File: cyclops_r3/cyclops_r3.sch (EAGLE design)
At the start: 133 parts, among them Q1 BC817, Q2 IRF510, U1 MCP4921, U10 TLV2374, U11 THS4281, U12 MAX4564, U13 ZXTD45, U14 ZXTD45, U2 ADG3301, U3 MCP4022-50k, U4 LT1931, U5 317-N, U6 337L, U7 TLV3701, U8 ADR03, U9 OP1177, X1 SLP3, X2 SLP3, X3 SLP3

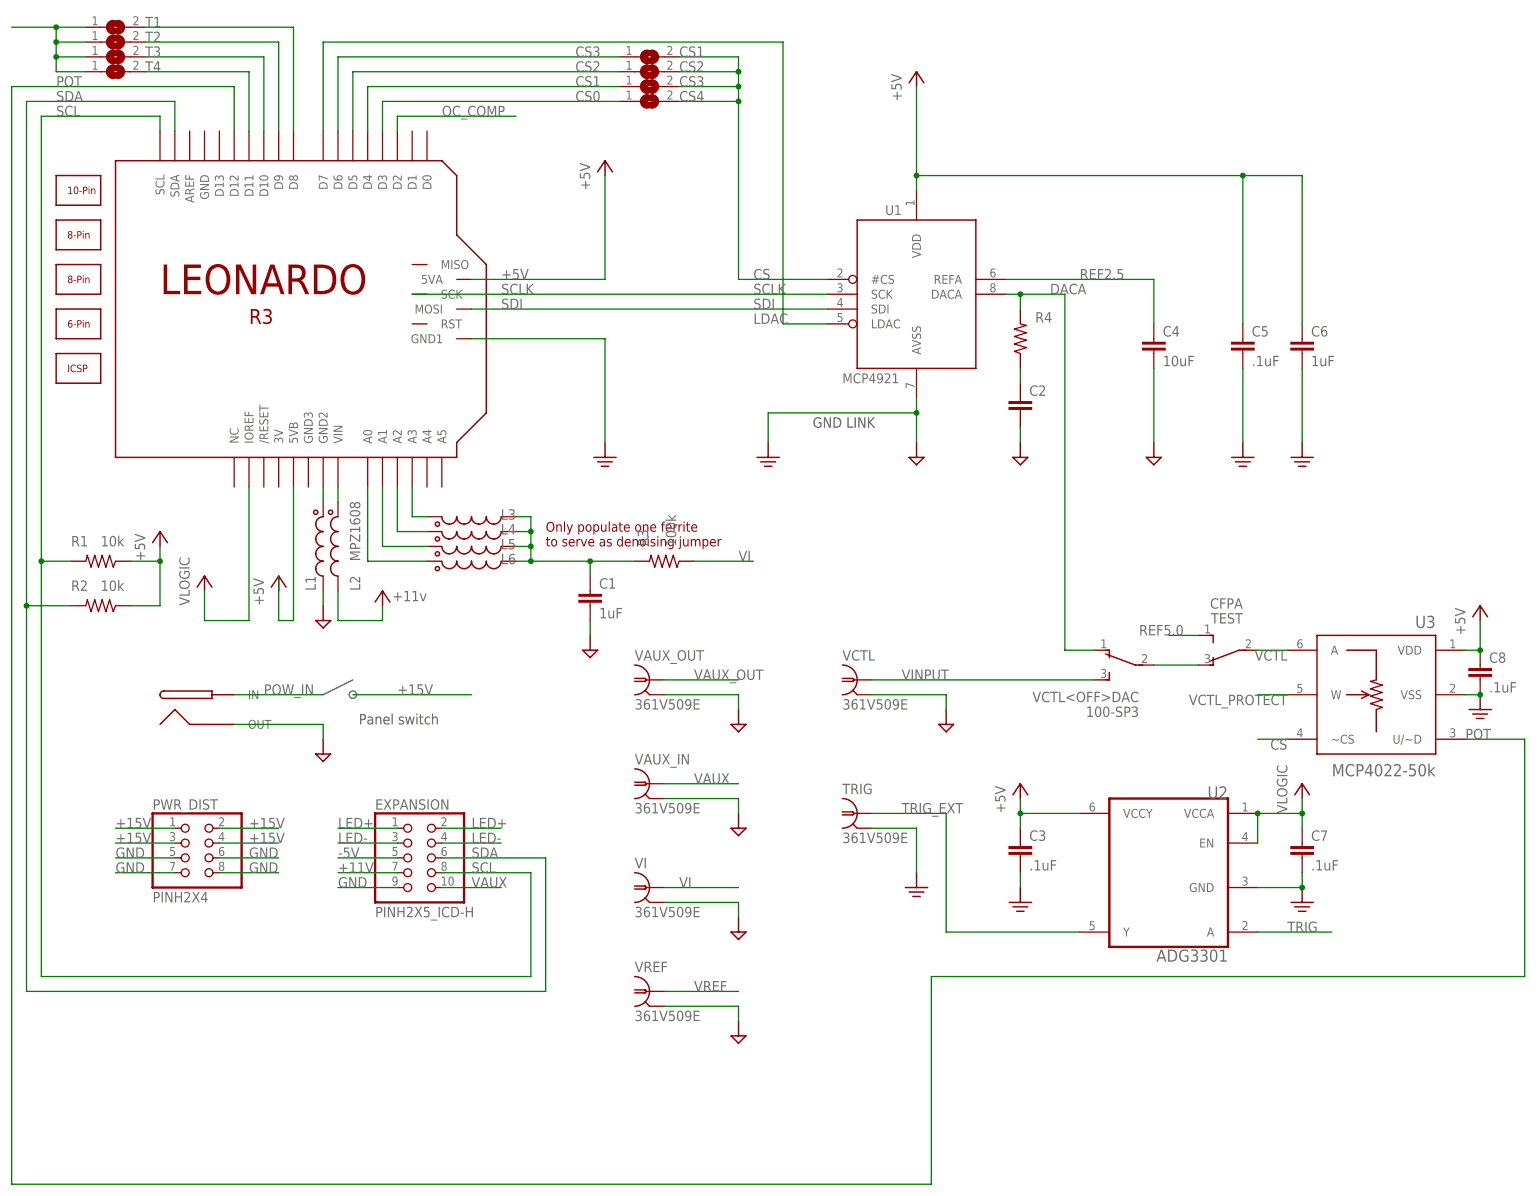
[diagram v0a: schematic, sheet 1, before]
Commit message: Almost ready to fabricate PCB. I need to do one last look over, concentrating on schematic.
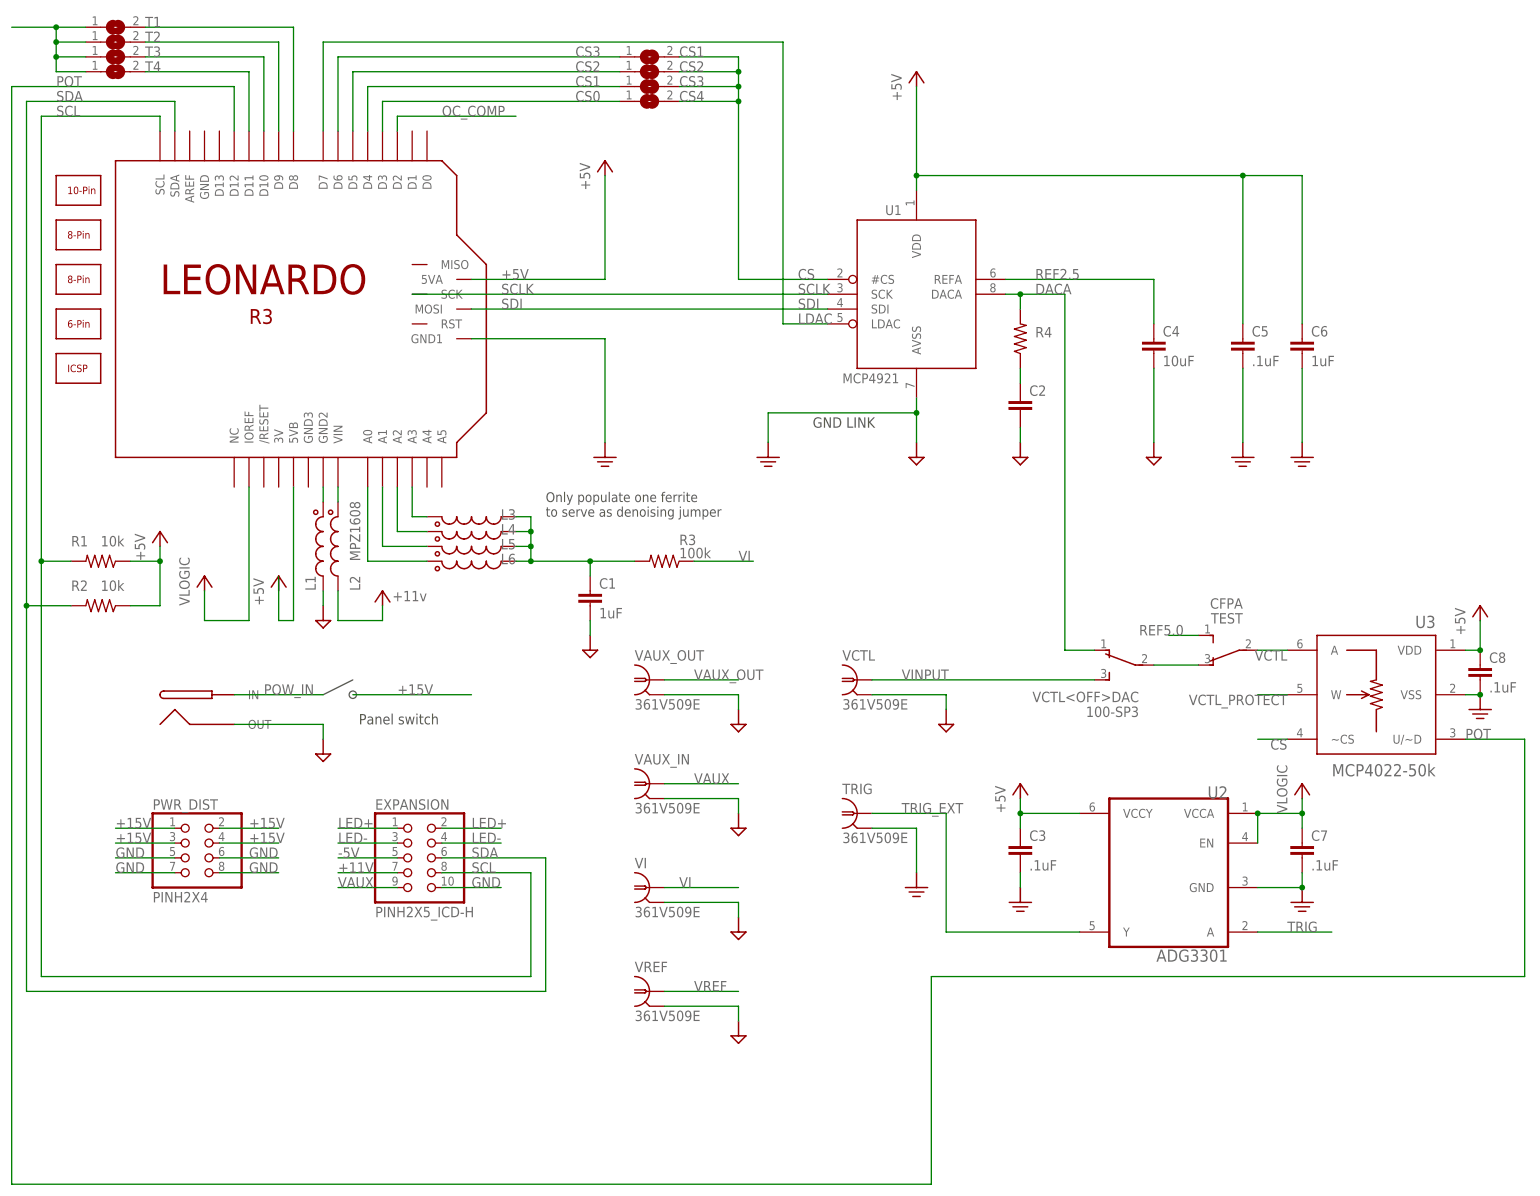
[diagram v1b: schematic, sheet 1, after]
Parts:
- NEG_SUPPLY: device jumper:SJ2W -> cyclops:SJ2W
- renumbered AUX<->CURR to AUX<>CURR
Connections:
- net +11V: now also AUX<>CURR.3; no longer AUX<>CURR.1
- net GND: now also AUX<>CURR.1, EXPANSION.10; no longer AUX<>CURR.3, EXPANSION.9
- net VAUX: now also EXPANSION.9; no longer EXPANSION.10
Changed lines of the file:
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@@
 <?xml version="1.0" encoding="utf-8"?>
 <!DOCTYPE eagle SYSTEM "eagle.dtd">
-<eagle version="6.6.0">
+<eagle version="6.5.0">
 <drawing>
 <settings>
@@
 <part name="D4" library="cyclops" deviceset="S-DIODE" device="SOD-123" value="DS11015"/>
 <part name="D3" library="cyclops" deviceset="S-DIODE" device="SOD-123" value="DS11015"/>
-<part name="AUX&lt;-&gt;CURR" library="cyclops" deviceset="SPDT" device="_JS" value="JS102"/>
+<part name="AUX&lt;&gt;CURR" library="cyclops" deviceset="SPDT" device="_JS" value="JS102"/>
 <part name="FRAME1" library="cyclops" deviceset="FRAME_A_L" device=""/>
 <part name="FRAME2" library="cyclops" deviceset="FRAME_A_L" device=""/>
@@
 <part name="U$52" library="cyclops" deviceset="GND2" device=""/>
 <part name="P+13" library="cyclops" deviceset="+5V" device="" value="+5V"/>
-<part name="NEG_SUPPLY" library="jumper" deviceset="SJ2W" device=""/>
+<part name="NEG_SUPPLY" library="cyclops" deviceset="SJ2W" device=""/>
 <part name="P+15" library="cyclops" deviceset="+5V" device="" value="+5V"/>
 <part name="C9" library="cyclops" deviceset="C" device="_0805" value="4.7uF"/>
@@
 <plain>
 <text x="137.16" y="63.5" size="1.778" layer="97">GND LINK</text>
-<text x="91.44" y="43.18" size="1.6764" layer="94">Only populate one ferrite
+<text x="91.44" y="48.26" size="1.6764" layer="97">Only populate one ferrite
 to serve as denoising jumper</text>
 <text x="193.04" y="129.54" size="3.81" layer="98">Input and output</text>
@@
 <instance part="C2" gate="C" x="172.72" y="68.58"/>
 <instance part="R4" gate="R" x="172.72" y="78.74" smashed="yes" rot="R90">
-<attribute name="NAME" x="175.26" y="81.5086" size="1.778" layer="95"/>
+<attribute name="NAME" x="175.26" y="78.9686" size="1.778" layer="95"/>
 <attribute name="VALUE" x="175.26" y="76.708" size="1.778" layer="96"/>
 </instance>
@@
 </instance>
 <instance part="R3" gate="R" x="111.76" y="40.64" smashed="yes" rot="R180">
-<attribute name="NAME" x="108.9914" y="43.18" size="1.778" layer="95" rot="R90"/>
-<attribute name="VALUE" x="113.792" y="43.18" size="1.778" layer="96" rot="R90"/>
+<attribute name="NAME" x="114.3" y="43.4086" size="1.778" layer="95"/>
+<attribute name="VALUE" x="114.3" y="41.148" size="1.778" layer="96"/>
 </instance>
 <instance part="C1" gate="C" x="99.06" y="35.56"/>
@@
 <label x="83.82" y="86.36" size="1.778" layer="95"/>
 <pinref part="U1" gate="G$1" pin="SCK"/>
-<label x="127" y="86.36" size="1.778" layer="95"/>
+<label x="134.62" y="86.36" size="1.778" layer="95"/>
 </segment>
 </net>
@@
 <label x="83.82" y="83.82" size="1.778" layer="95"/>
 <pinref part="U1" gate="G$1" pin="SDI"/>
-<label x="127" y="83.82" size="1.778" layer="95"/>
+<label x="134.62" y="83.82" size="1.778" layer="95"/>
 </segment>
 </net>
@@
 <pinref part="U1" gate="G$1" pin="LDAC"/>
 <wire x1="139.7" y1="81.28" x2="132.08" y2="81.28" width="0.1524" layer="91"/>
-<label x="127" y="81.28" size="1.778" layer="95"/>
+<label x="134.62" y="81.28" size="1.778" layer="95"/>
 <wire x1="132.08" y1="81.28" x2="132.08" y2="129.54" width="0.1524" layer="91"/>
 <wire x1="132.08" y1="129.54" x2="53.34" y2="129.54" width="0.1524" layer="91"/>
@@
 <pinref part="U1" gate="G$1" pin="#CS"/>
 <wire x1="139.7" y1="88.9" x2="124.46" y2="88.9" width="0.1524" layer="91"/>
-<label x="127" y="88.9" size="1.778" layer="95"/>
+<label x="134.62" y="88.9" size="1.778" layer="95"/>
 <wire x1="114.3" y1="127" x2="124.46" y2="127" width="0.1524" layer="91"/>
 <wire x1="124.46" y1="127" x2="124.46" y2="124.46" width="0.1524" layer="91"/>
@@
 <segment>
 <pinref part="U1" gate="G$1" pin="DACA"/>
-<label x="177.8" y="86.36" size="1.778" layer="95"/>
+<label x="175.26" y="86.36" size="1.778" layer="95"/>
 <wire x1="170.18" y1="86.36" x2="172.72" y2="86.36" width="0.1524" layer="91"/>
 <wire x1="172.72" y1="86.36" x2="180.34" y2="86.36" width="0.1524" layer="91"/>
@@
 </segment>
 <segment>
-<pinref part="EXPANSION" gate="G$1" pin="9"/>
-<wire x1="66.04" y1="-15.24" x2="55.88" y2="-15.24" width="0.1524" layer="91"/>
-<label x="55.88" y="-15.24" size="1.778" layer="95"/>
-</segment>
-<segment>
 <pinref part="C1" gate="C" pin="2"/>
 <wire x1="99.06" y1="30.48" x2="99.06" y2="27.94" width="0.1524" layer="91"/>
@@
 <label x="17.78" y="-10.16" size="1.778" layer="95"/>
 </segment>
+<segment>
+<pinref part="EXPANSION" gate="G$1" pin="10"/>
+<wire x1="73.66" y1="-15.24" x2="83.82" y2="-15.24" width="0.1524" layer="91"/>
+<label x="78.74" y="-15.24" size="1.778" layer="95"/>
+</segment>
 </net>
 <net name="VAUX" class="0">
@@
 </segment>
 <segment>
-<pinref part="EXPANSION" gate="G$1" pin="10"/>
-<wire x1="73.66" y1="-15.24" x2="83.82" y2="-15.24" width="0.1524" layer="91"/>
-<label x="78.74" y="-15.24" size="1.778" layer="95"/>
+<pinref part="EXPANSION" gate="G$1" pin="9"/>
+<wire x1="66.04" y1="-15.24" x2="55.88" y2="-15.24" width="0.1524" layer="91"/>
+<label x="55.88" y="-15.24" size="1.778" layer="95"/>
 </segment>
 </net>
@@
 <pinref part="U1" gate="G$1" pin="REFA"/>
 <wire x1="170.18" y1="88.9" x2="195.58" y2="88.9" width="0.1524" layer="91"/>
-<label x="182.88" y="88.9" size="1.778" layer="95"/>
+<label x="175.26" y="88.9" size="1.778" layer="95"/>
 <pinref part="C4" gate="C" pin="1"/>
 <wire x1="195.58" y1="81.28" x2="195.58" y2="88.9" width="0.1524" layer="91"/>
@@
 <attribute name="NAME" x="58.42" y="-72.39" size="1.778" layer="95" rot="R180"/>
 </instance>
-<instance part="NEG_SUPPLY" gate="G$1" x="-88.9" y="-66.04" rot="R180"/>
+<instance part="NEG_SUPPLY" gate="G$1" x="-88.9" y="-66.04" smashed="yes" rot="R180">
+<attribute name="NAME" x="-85.979" y="-68.58" size="1.778" layer="95" rot="R270"/>
+<attribute name="VALUE" x="-91.44" y="-64.135" size="1.778" layer="96" rot="R180"/>
+</instance>
 <instance part="P+15" gate="1" x="-101.6" y="-66.04"/>
 <instance part="C9" gate="C" x="-78.74" y="-88.9"/>
@@
 <instance part="D4" gate="G$1" x="-10.16" y="73.66" rot="R90"/>
 <instance part="D3" gate="G$1" x="-10.16" y="99.06" rot="R90"/>
-<instance part="AUX&lt;-&gt;CURR" gate="G$1" x="48.26" y="17.78"/>
+<instance part="AUX&lt;&gt;CURR" gate="G$1" x="48.26" y="17.78" smashed="yes" rot="MR180">
+<attribute name="NAME" x="38.1" y="13.97" size="1.778" layer="95" rot="MR180"/>
+<attribute name="VALUE" x="43.18" y="16.51" size="1.778" layer="96" rot="MR180"/>
+</instance>
 <instance part="FRAME4" gate="G$1" x="-91.44" y="-58.42"/>
 <instance part="U14" gate="G$1" x="119.38" y="83.82"/>
@@
 </segment>
 <segment>
-<pinref part="AUX&lt;-&gt;CURR" gate="G$1" pin="3"/>
-<wire x1="55.88" y1="15.24" x2="55.88" y2="12.7" width="0.1524" layer="91"/>
-</segment>
-<segment>
 <wire x1="50.8" y1="68.58" x2="50.8" y2="63.5" width="0.1524" layer="91"/>
 <pinref part="R26" gate="R" pin="2"/>
@@
 <pinref part="C35" gate="C" pin="2"/>
 <wire x1="43.18" y1="96.52" x2="43.18" y2="93.98" width="0.1524" layer="91"/>
+</segment>
+<segment>
+<pinref part="AUX&lt;&gt;CURR" gate="G$1" pin="1"/>
+<wire x1="55.88" y1="15.24" x2="55.88" y2="12.7" width="0.1524" layer="91"/>
 </segment>
 </net>
@@
 </segment>
 <segment>
-<pinref part="AUX&lt;-&gt;CURR" gate="G$1" pin="1"/>
+<pinref part="AUX&lt;&gt;CURR" gate="G$1" pin="3"/>
 <wire x1="55.88" y1="20.32" x2="55.88" y2="22.86" width="0.1524" layer="91"/>
 </segment>
@@
 <net name="IN" class="0">
 <segment>
-<pinref part="AUX&lt;-&gt;CURR" gate="G$1" pin="2"/>
+<pinref part="AUX&lt;&gt;CURR" gate="G$1" pin="2"/>
 <wire x1="45.72" y1="17.78" x2="43.18" y2="17.78" width="0.1524" layer="91"/>
 <pinref part="U12" gate="G$1" pin="IN"/>

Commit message: Minor.
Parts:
- RSENSE: value 0.25,2W -> 1R0,2W
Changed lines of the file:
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@@
 <part name="R27" library="cyclops" deviceset="R" device="_0603" value="3k"/>
 <part name="R28" library="cyclops" deviceset="R" device="_0603" value="1k"/>
-<part name="RSENSE" library="cyclops" deviceset="R" device="_2512" value="0.25,2W"/>
+<part name="RSENSE" library="cyclops" deviceset="R" device="_2512" value="1R0,2W"/>
 <part name="U8" library="cyclops" deviceset="ADR03AKSZ-REEL7" device="" value="ADR03"/>
 <part name="C22" library="cyclops" deviceset="C" device="_0805" value="1uF"/>
